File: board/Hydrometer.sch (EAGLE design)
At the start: 15 parts, among them IC2 REG1117

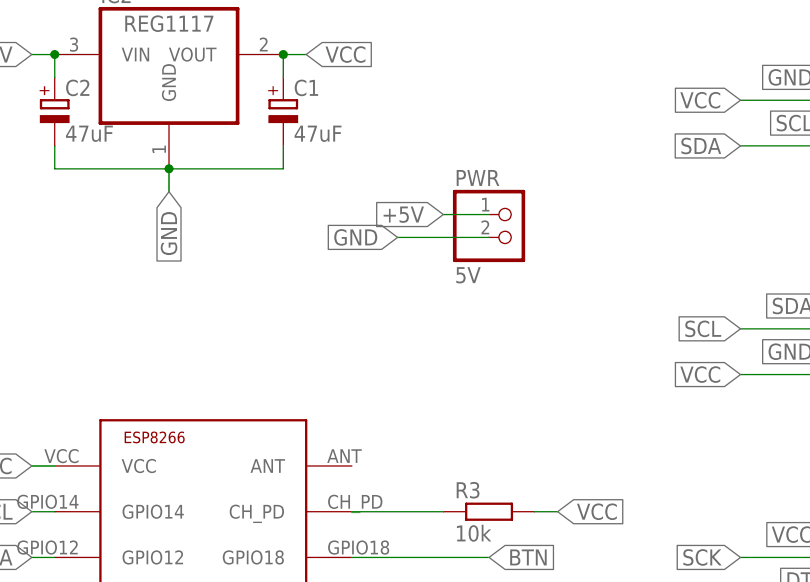
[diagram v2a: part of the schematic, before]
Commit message: Add input protection and power LED
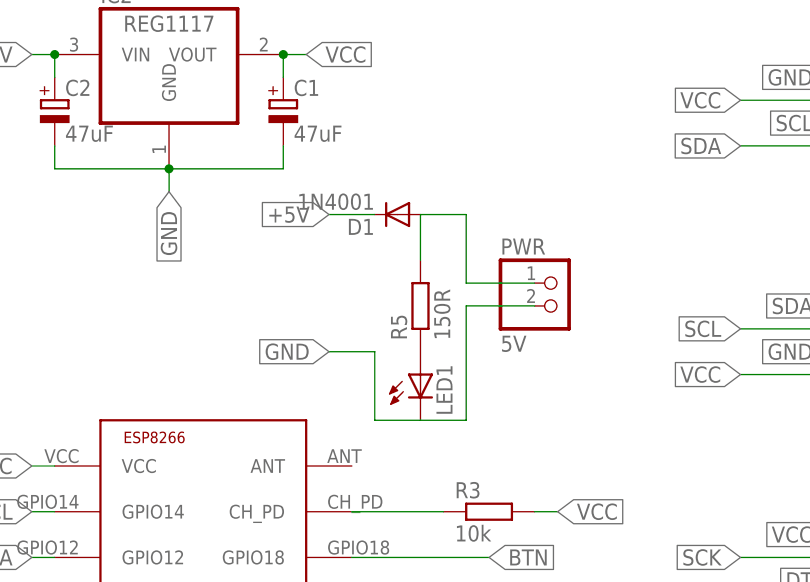
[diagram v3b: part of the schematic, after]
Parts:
- added D1: 1N4001, diode:1N4004
- added LED1: (no value), led:LED3MM
- added R5: 150R, resistor:R-EU_0204/7
- R2: device resistor:R-EU_R1206 -> resistor:R-EU_0204/7
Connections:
- new net N$4: D1.A, PWR.1, R5.2
- new net N$8: LED1.A, R5.1
- net +5V: now also D1.C; no longer PWR.1
- net GND: now also LED1.C
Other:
- moved on the sheet: PWR
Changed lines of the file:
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@@
 <grid distance="0.1" unitdist="inch" unit="inch" style="lines" multiple="1" display="no" altdistance="0.01" altunitdist="inch" altunit="inch"/>
 <layers>
-<layer number="1" name="Top" color="4" fill="1" visible="no" active="no"/>
-<layer number="16" name="Bottom" color="1" fill="1" visible="no" active="no"/>
-<layer number="17" name="Pads" color="2" fill="1" visible="no" active="no"/>
-<layer number="18" name="Vias" color="2" fill="1" visible="no" active="no"/>
-<layer number="19" name="Unrouted" color="6" fill="1" visible="no" active="no"/>
-<layer number="20" name="Dimension" color="15" fill="1" visible="no" active="no"/>
-<layer number="21" name="tPlace" color="7" fill="1" visible="no" active="no"/>
-<layer number="22" name="bPlace" color="7" fill="1" visible="no" active="no"/>
-<layer number="23" name="tOrigins" color="15" fill="1" visible="no" active="no"/>
-<layer number="24" name="bOrigins" color="15" fill="1" visible="no" active="no"/>
-<layer number="25" name="tNames" color="7" fill="1" visible="no" active="no"/>
-<layer number="26" name="bNames" color="7" fill="1" visible="no" active="no"/>
-<layer number="27" name="tValues" color="7" fill="1" visible="no" active="no"/>
-<layer number="28" name="bValues" color="7" fill="1" visible="no" active="no"/>
+<layer number="1" name="Top" color="4" fill="1" visible="yes" active="no"/>
+<layer number="16" name="Bottom" color="1" fill="1" visible="yes" active="no"/>
+<layer number="17" name="Pads" color="2" fill="1" visible="yes" active="no"/>
+<layer number="18" name="Vias" color="2" fill="1" visible="yes" active="no"/>
+<layer number="19" name="Unrouted" color="6" fill="1" visible="yes" active="no"/>
+<layer number="20" name="Dimension" color="15" fill="1" visible="yes" active="no"/>
+<layer number="21" name="tPlace" color="7" fill="1" visible="yes" active="no"/>
+<layer number="22" name="bPlace" color="7" fill="1" visible="yes" active="no"/>
+<layer number="23" name="tOrigins" color="15" fill="1" visible="yes" active="no"/>
+<layer number="24" name="bOrigins" color="15" fill="1" visible="yes" active="no"/>
+<layer number="25" name="tNames" color="7" fill="1" visible="yes" active="no"/>
+<layer number="26" name="bNames" color="7" fill="1" visible="yes" active="no"/>
+<layer number="27" name="tValues" color="7" fill="1" visible="yes" active="no"/>
+<layer number="28" name="bValues" color="7" fill="1" visible="yes" active="no"/>
 <layer number="29" name="tStop" color="7" fill="3" visible="no" active="no"/>
 <layer number="30" name="bStop" color="7" fill="6" visible="no" active="no"/>
@@
 <layer number="35" name="tGlue" color="7" fill="4" visible="no" active="no"/>
 <layer number="36" name="bGlue" color="7" fill="5" visible="no" active="no"/>
-<layer number="37" name="tTest" color="7" fill="1" visible="no" active="no"/>
-<layer number="38" name="bTest" color="7" fill="1" visible="no" active="no"/>
+<layer number="37" name="tTest" color="7" fill="1" visible="yes" active="no"/>
+<layer number="38" name="bTest" color="7" fill="1" visible="yes" active="no"/>
 <layer number="39" name="tKeepout" color="4" fill="11" visible="no" active="no"/>
 <layer number="40" name="bKeepout" color="1" fill="11" visible="no" active="no"/>
@@
 <layer number="44" name="Drills" color="7" fill="1" visible="no" active="no"/>
 <layer number="45" name="Holes" color="7" fill="1" visible="no" active="no"/>
-<layer number="46" name="Milling" color="3" fill="1" visible="no" active="no"/>
-<layer number="47" name="Measures" color="7" fill="1" visible="no" active="no"/>
-<layer number="48" name="Document" color="7" fill="1" visible="no" active="no"/>
-<layer number="49" name="Reference" color="7" fill="1" visible="no" active="no"/>
-<layer number="51" name="tDocu" color="7" fill="1" visible="no" active="no"/>
-<layer number="52" name="bDocu" color="7" fill="1" visible="no" active="no"/>
+<layer number="46" name="Milling" color="3" fill="1" visible="yes" active="no"/>
+<layer number="47" name="Measures" color="7" fill="1" visible="yes" active="no"/>
+<layer number="48" name="Document" color="7" fill="1" visible="yes" active="no"/>
+<layer number="49" name="Reference" color="7" fill="1" visible="yes" active="no"/>
+<layer number="51" name="tDocu" color="7" fill="1" visible="yes" active="no"/>
+<layer number="52" name="bDocu" color="7" fill="1" visible="yes" active="no"/>
 <layer number="90" name="Modules" color="5" fill="1" visible="yes" active="yes"/>
 <layer number="91" name="Nets" color="2" fill="1" visible="yes" active="yes"/>
@@
 <part name="PWR" library="pinhead" deviceset="PINHD-1X2" device="" value="5V"/>
 <part name="R1" library="resistor" deviceset="R-EU_" device="R1206" value="10k"/>
-<part name="R2" library="resistor" deviceset="R-EU_" device="R1206" value="10k"/>
+<part name="R2" library="resistor" deviceset="R-EU_" device="0204/7" value="10k"/>
 <part name="R3" library="resistor" deviceset="R-EU_" device="R1206" value="10k"/>
 <part name="C1" library="resistor" deviceset="CPOL-EU" device="E2-5" value="47uF"/>
@@
 <part name="R4" library="resistor" deviceset="R-EU_" device="R1206" value="10k"/>
 <part name="JP2" library="pinhead" deviceset="PINHD-1X3" device="" value="MODE"/>
+<part name="D1" library="diode" deviceset="1N4004" device="" value="1N4001"/>
+<part name="R5" library="resistor" deviceset="R-EU_" device="0204/7" value="150R"/>
+<part name="LED1" library="led" deviceset="LED" device="3MM"/>
 </parts>
 <sheets>
@@
 <instance part="HX711" gate="A" x="55.88" y="60.96"/>
 <instance part="S1" gate="1" x="48.26" y="30.48" rot="R270"/>
-<instance part="PWR" gate="G$1" x="12.7" y="99.06"/>
+<instance part="PWR" gate="G$1" x="17.78" y="91.44"/>
 <instance part="R1" gate="G$1" x="-55.88" y="53.34"/>
 <instance part="R2" gate="G$1" x="-48.26" y="43.18"/>
@@
 <instance part="R4" gate="G$1" x="38.1" y="38.1" rot="R90"/>
 <instance part="JP2" gate="A" x="-58.42" y="43.18"/>
+<instance part="D1" gate="1" x="0" y="101.6" rot="R180"/>
+<instance part="R5" gate="G$1" x="2.54" y="91.44" rot="R90"/>
+<instance part="LED1" gate="G$1" x="2.54" y="83.82"/>
 </instances>
 <busses>
@@
 </segment>
 <segment>
-<pinref part="PWR" gate="G$1" pin="2"/>
-<wire x1="10.16" y1="99.06" x2="0" y2="99.06" width="0.1524" layer="91"/>
-<label x="0" y="99.06" size="1.778" layer="95" rot="MR0" xref="yes"/>
-</segment>
-<segment>
 <pinref part="R1" gate="G$1" pin="1"/>
 <wire x1="-60.96" y1="53.34" x2="-63.5" y2="53.34" width="0.1524" layer="91"/>
@@
 <wire x1="-60.96" y1="40.64" x2="-68.58" y2="40.64" width="0.1524" layer="91"/>
 <label x="-68.58" y="40.64" size="1.778" layer="95" rot="MR0" xref="yes"/>
+</segment>
+<segment>
+<pinref part="PWR" gate="G$1" pin="2"/>
+<wire x1="15.24" y1="91.44" x2="7.62" y2="91.44" width="0.1524" layer="91"/>
+<wire x1="7.62" y1="91.44" x2="7.62" y2="78.74" width="0.1524" layer="91"/>
+<pinref part="LED1" gate="G$1" pin="C"/>
+<wire x1="7.62" y1="78.74" x2="2.54" y2="78.74" width="0.1524" layer="91"/>
+<wire x1="2.54" y1="78.74" x2="-2.54" y2="78.74" width="0.1524" layer="91"/>
+<wire x1="-2.54" y1="78.74" x2="-2.54" y2="86.36" width="0.1524" layer="91"/>
+<wire x1="-2.54" y1="86.36" x2="-7.62" y2="86.36" width="0.1524" layer="91"/>
+<label x="-7.62" y="86.36" size="1.778" layer="95" rot="MR0" xref="yes"/>
 </segment>
 </net>
@@
 </segment>
 <segment>
-<pinref part="PWR" gate="G$1" pin="1"/>
-<wire x1="10.16" y1="101.6" x2="5.08" y2="101.6" width="0.1524" layer="91"/>
-<label x="5.08" y="101.6" size="1.778" layer="95" rot="MR0" xref="yes"/>
+<pinref part="D1" gate="1" pin="C"/>
+<wire x1="-2.54" y1="101.6" x2="-7.62" y2="101.6" width="0.1524" layer="91"/>
+<label x="-7.62" y="101.6" size="1.778" layer="95" rot="MR0" xref="yes"/>
 </segment>
 </net>
@@
 </segment>
 </net>
+<net name="N$8" class="0">
+<segment>
+<pinref part="R5" gate="G$1" pin="1"/>
+<pinref part="LED1" gate="G$1" pin="A"/>
+</segment>
+</net>
+<net name="N$4" class="0">
+<segment>
+<pinref part="PWR" gate="G$1" pin="1"/>
+<wire x1="15.24" y1="93.98" x2="7.62" y2="93.98" width="0.1524" layer="91"/>
+<wire x1="7.62" y1="93.98" x2="7.62" y2="101.6" width="0.1524" layer="91"/>
+<pinref part="D1" gate="1" pin="A"/>
+<wire x1="7.62" y1="101.6" x2="2.54" y2="101.6" width="0.1524" layer="91"/>
+<pinref part="R5" gate="G$1" pin="2"/>
+<wire x1="2.54" y1="101.6" x2="2.54" y2="96.52" width="0.1524" layer="91"/>
+</segment>
+</net>
